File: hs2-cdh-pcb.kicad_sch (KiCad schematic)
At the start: 15 parts, among them IC1 IS25LP01GJ-RMLE-TY, IC2 IS25LP01GJ-RMLE-TY, IC3 IS25LP01GJ-RMLE-TY, IC4 IS25LP01GJ-RMLE-TY, P8 BeagleBone_Black_Header, P9 BeagleBone_Black_Header, SW1 SW_DIP_x02, U1 CAT24C256

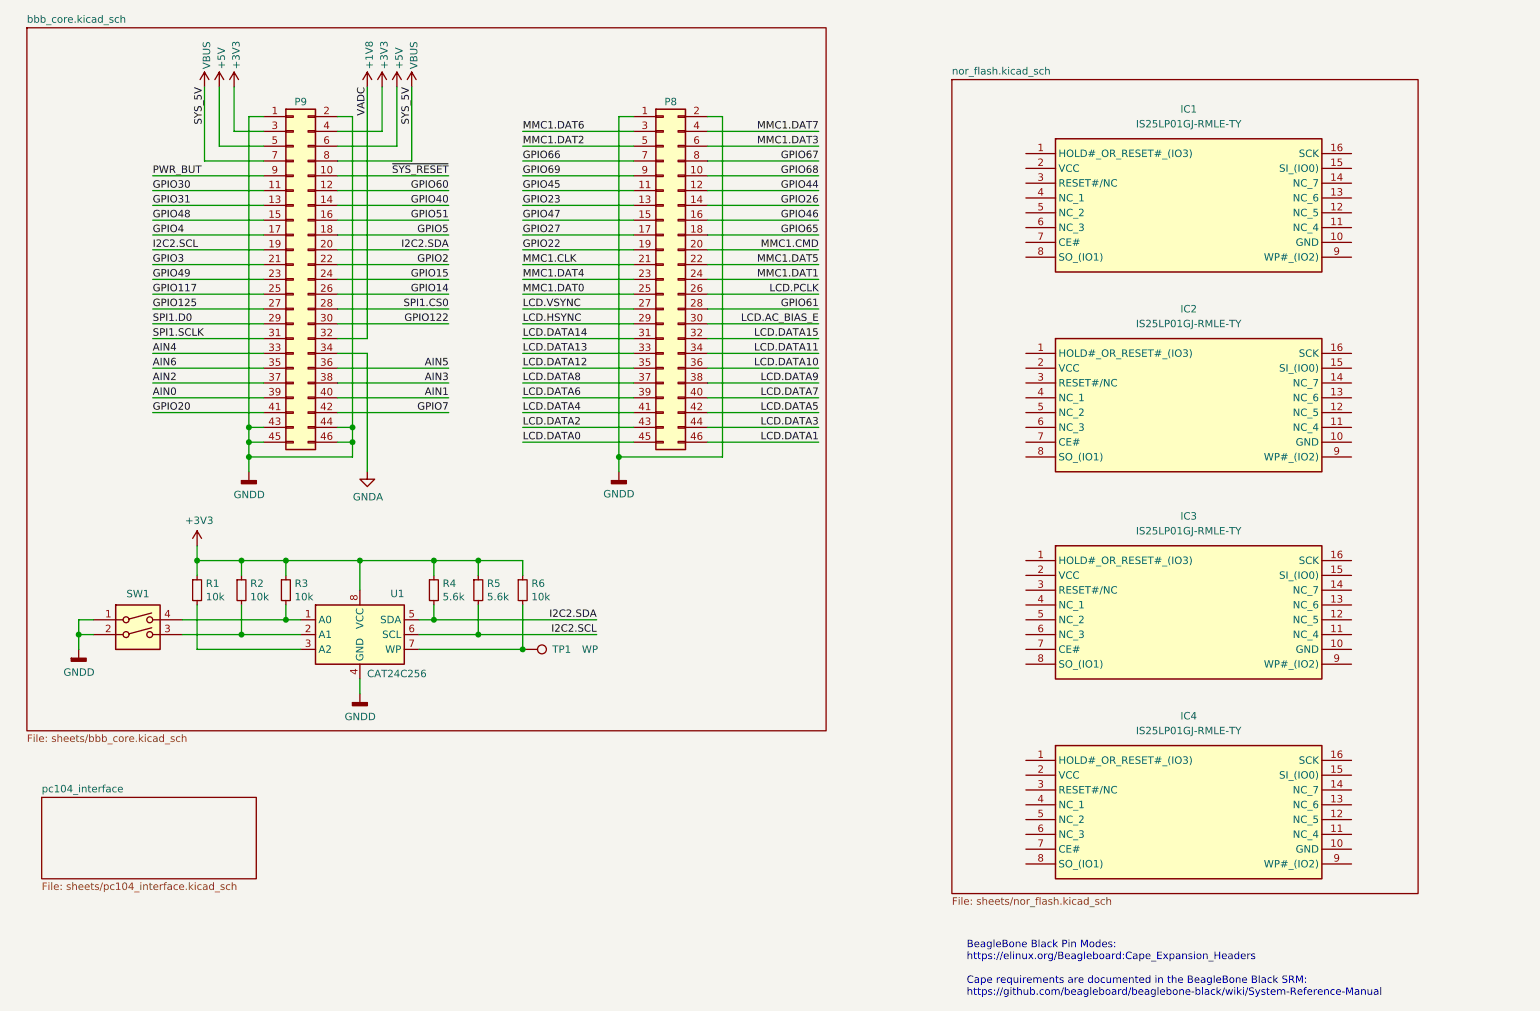
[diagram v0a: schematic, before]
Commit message: Pushing changes to top level after removing bbb cape and nor flash ics
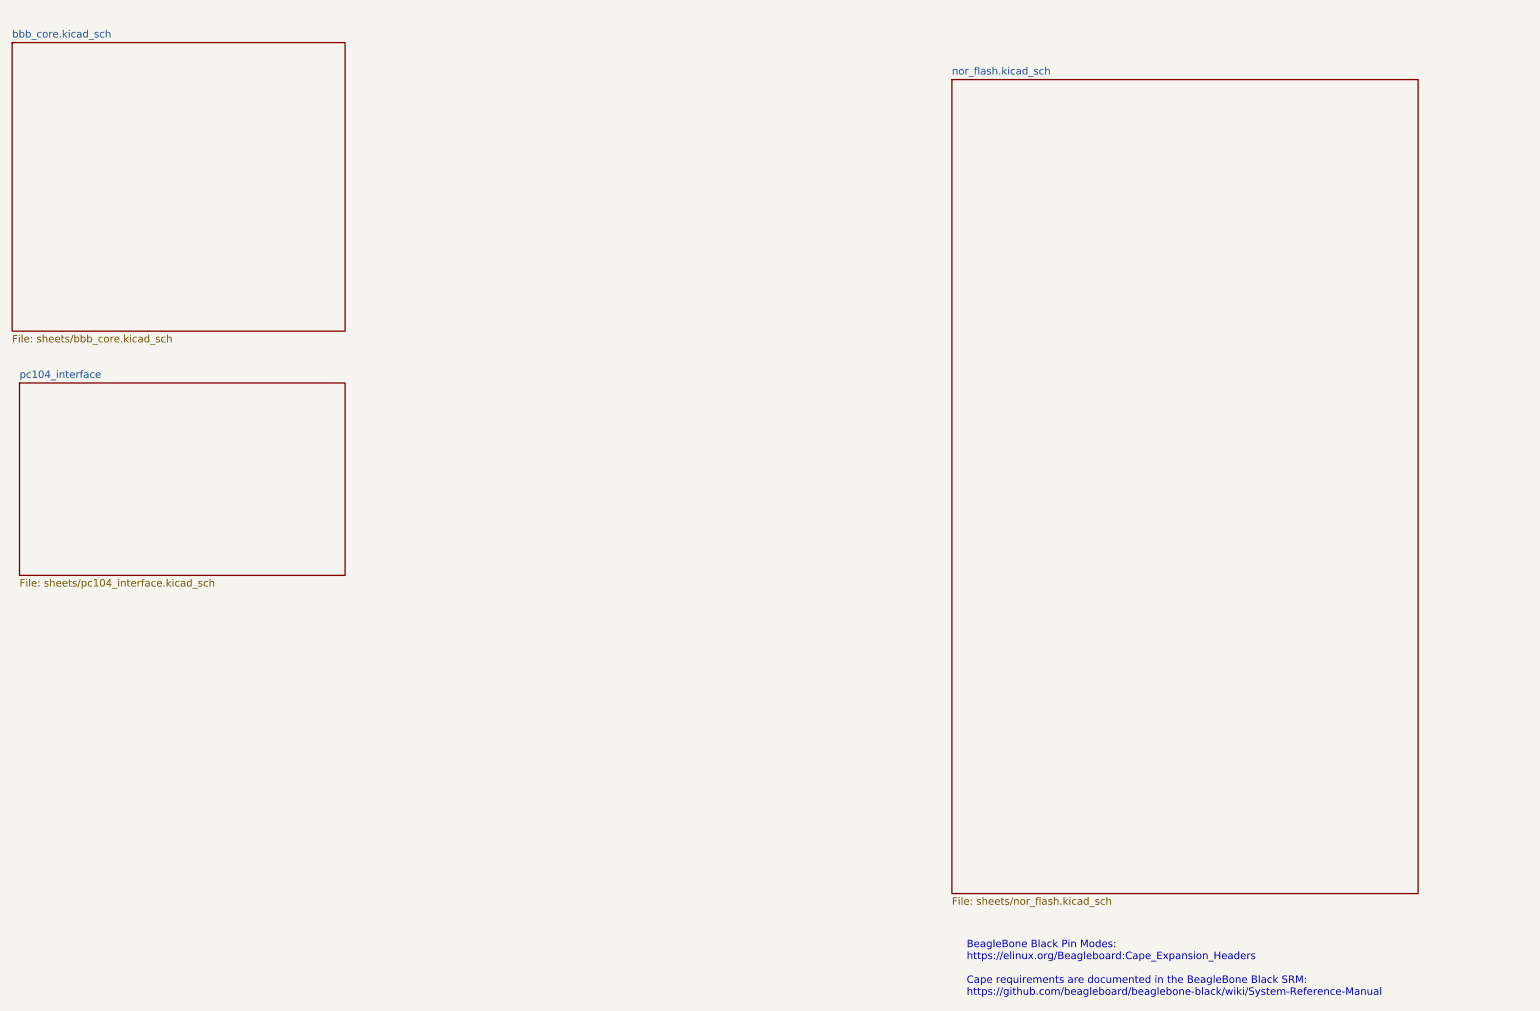
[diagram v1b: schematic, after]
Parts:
- removed IC1, IC2, IC3, IC4: IS25LP01GJ-RMLE-TY, SOIC127P1032X265-16N, symbol Memory Chip:IS25LP01GJ-RMLE-TY
- removed P8, P9: BeagleBone_Black_Header, Connector_PinHeader_2.54mm:PinHeader_2x23_P2.54mm_Vertical, symbol Connector_Generic:Conn_02x23_Odd_Even
- removed R1, R2, R3, R6: 10k, symbol Device:R_Small
- removed R4, R5: 5.6k, symbol Device:R_Small
- removed SW1: SW_DIP_x02, symbol Switch:SW_DIP_x02
- removed TP1: WP, symbol Connector:TestPoint
- removed U1: CAT24C256, symbol Memory_EEPROM:CAT24C256

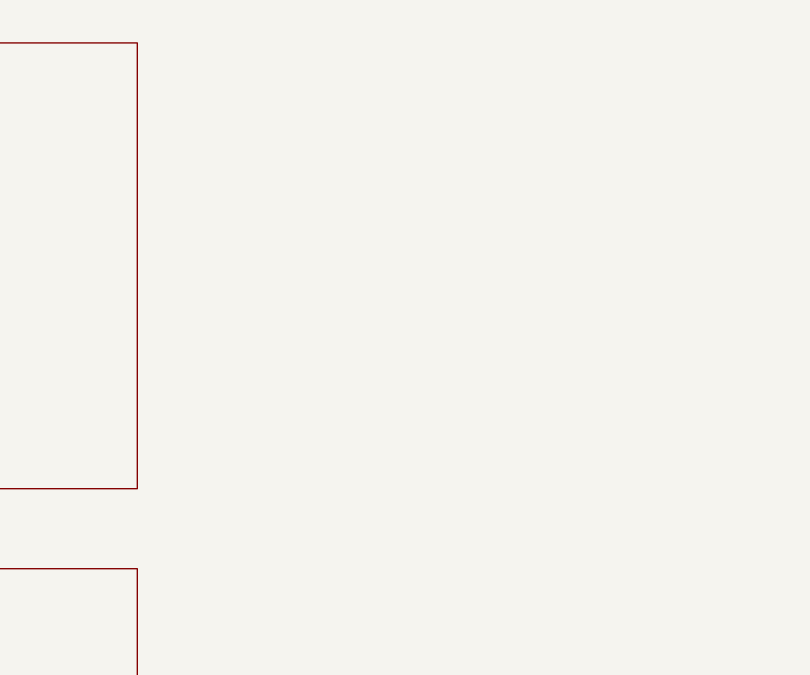
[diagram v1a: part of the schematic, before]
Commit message: Adding power distribution schematic
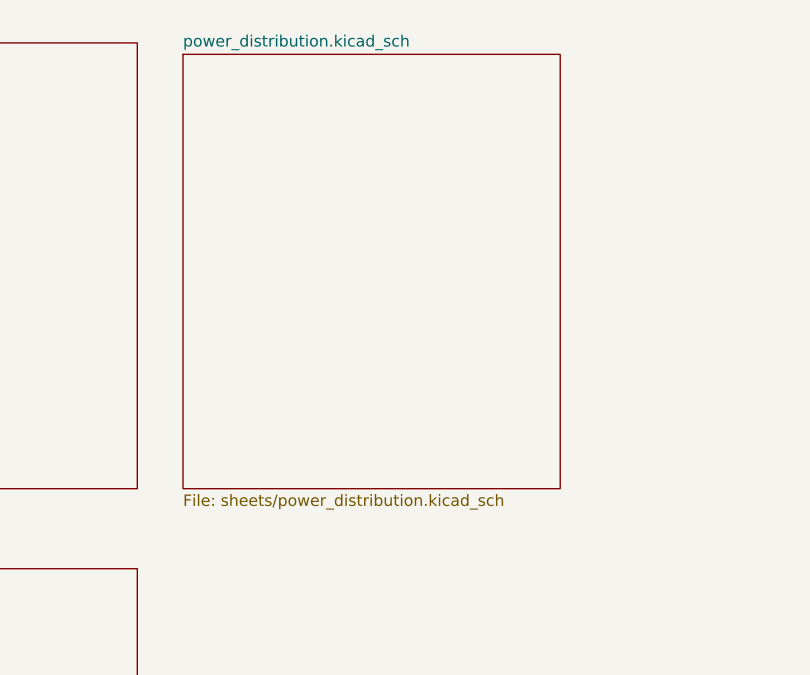
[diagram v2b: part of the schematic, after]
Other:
- added sheet power_distribution.kicad_sch (sheets/power_distribution.kicad_sch)
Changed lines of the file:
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@@
+	)
+	(sheet
+		(at 76.2 17.78)
+		(size 41.91 48.26)
+		(exclude_from_sim no)
+		(in_bom yes)
+		(on_board yes)
+		(dnp no)
+		(fields_autoplaced yes)
+		(stroke
+			(width 0.1524)
+			(type solid)
+		)
+		(fill
+			(color 0 0 0 0)
+		)
+		(property "Sheetname" "power_distribution.kicad_sch"
+			(at 76.2 17.0684 0)
+			(show_name no)
+			(do_not_autoplace no)
+			(effects
+				(font
+					(size 1.27 1.27)
+				)
+				(justify left bottom)
+			)
+		)
+		(property "Sheetfile" "sheets/power_distribution.kicad_sch"
+			(at 76.2 66.6246 0)
+			(show_name no)
+			(do_not_autoplace no)
+			(effects
+				(font
+					(size 1.27 1.27)
+				)
+				(justify left top)
+			)
+		)
+		(instances
+			(project "hs2-cdh-pcb"
+				(path "/e63e39d7-6ac0-4ffd-8aa3-1841a4541b55"
+					(page "5")
+				)
+			)
+		)
 	)
 	(sheet

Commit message: oops forgot to add all changes from prev commits
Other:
- added sheet thermal (sheets/thermal.kicad_sch)
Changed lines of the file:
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@@
+	)
+	(sheet
+		(at 78.74 75.946)
+		(size 49.022 33.02)
+		(exclude_from_sim no)
+		(in_bom yes)
+		(on_board yes)
+		(dnp no)
+		(fields_autoplaced yes)
+		(stroke
+			(width 0.1524)
+			(type solid)
+		)
+		(fill
+			(color 0 0 0 0)
+		)
+		(property "Sheetname" "thermal"
+			(at 78.74 75.2344 0)
+			(show_name no)
+			(do_not_autoplace no)
+			(effects
+				(font
+					(size 1.27 1.27)
+				)
+				(justify left bottom)
+			)
+		)
+		(property "Sheetfile" "sheets/thermal.kicad_sch"
+			(at 78.74 109.5506 0)
+			(show_name no)
+			(do_not_autoplace no)
+			(effects
+				(font
+					(size 1.27 1.27)
+				)
+				(justify left top)
+			)
+		)
+		(instances
+			(project "hs2-cdh-pcb"
+				(path "/e63e39d7-6ac0-4ffd-8aa3-1841a4541b55"
+					(page "6")
+				)
+			)
+		)
 	)
 	(sheet
